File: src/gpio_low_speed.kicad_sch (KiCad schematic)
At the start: 3 parts, among them J1 RJ45_Amphenol_RJMG1BD3B8K1ANR, J2 Micro_SD_Card_Det2

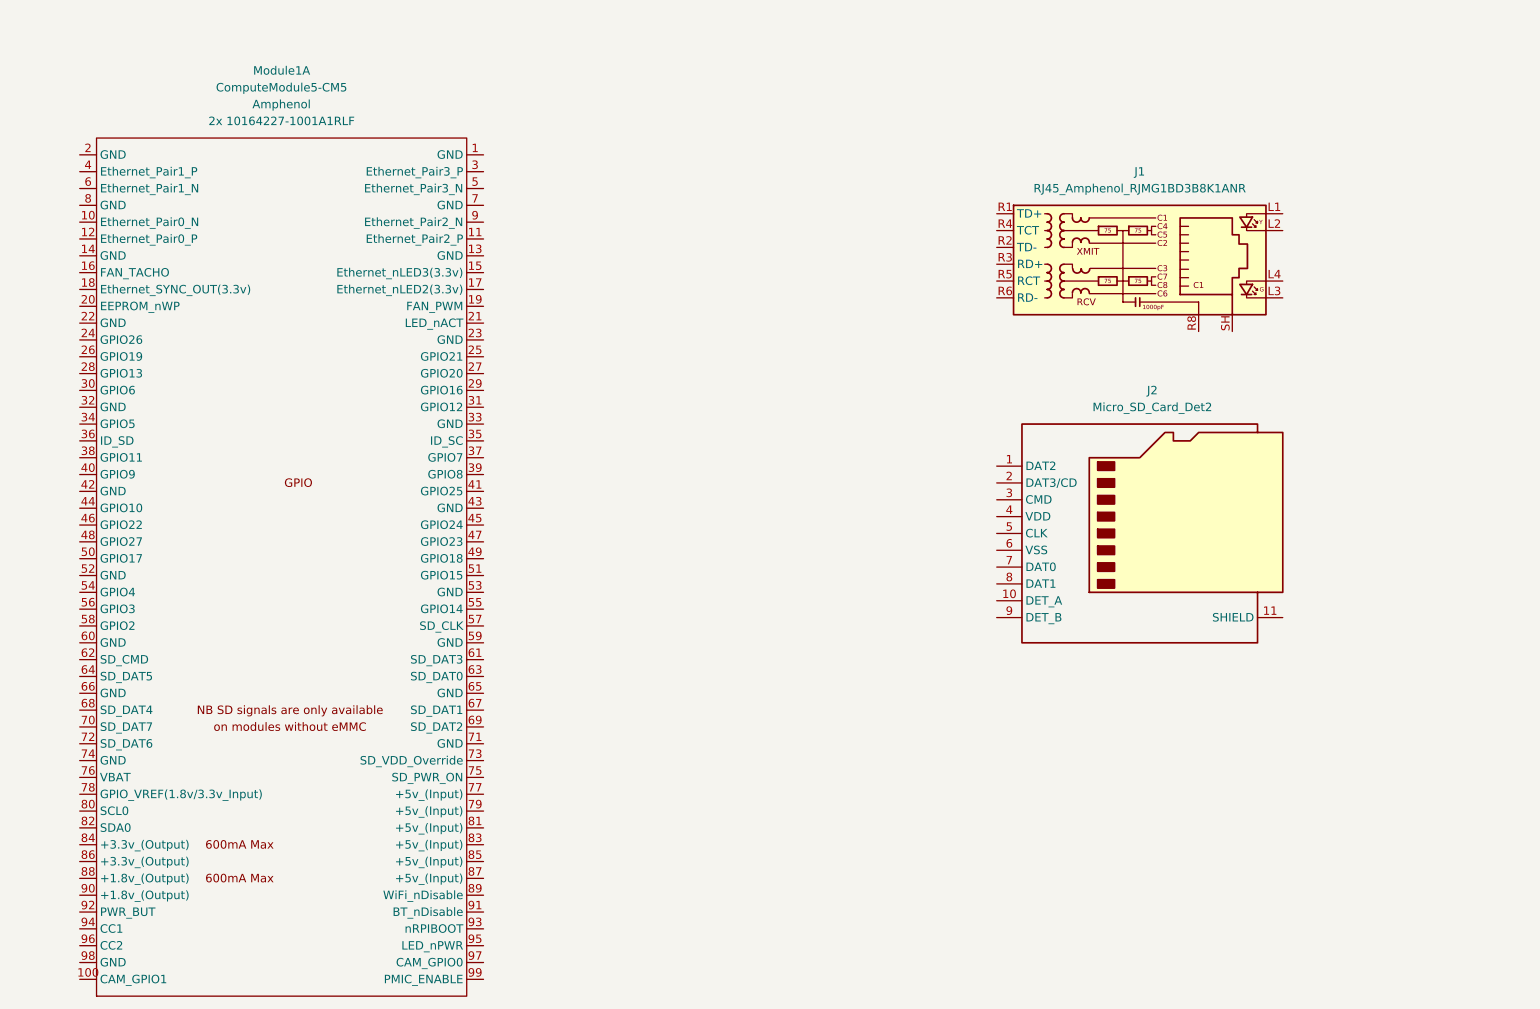
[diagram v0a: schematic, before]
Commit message: Add ethernet circuitry
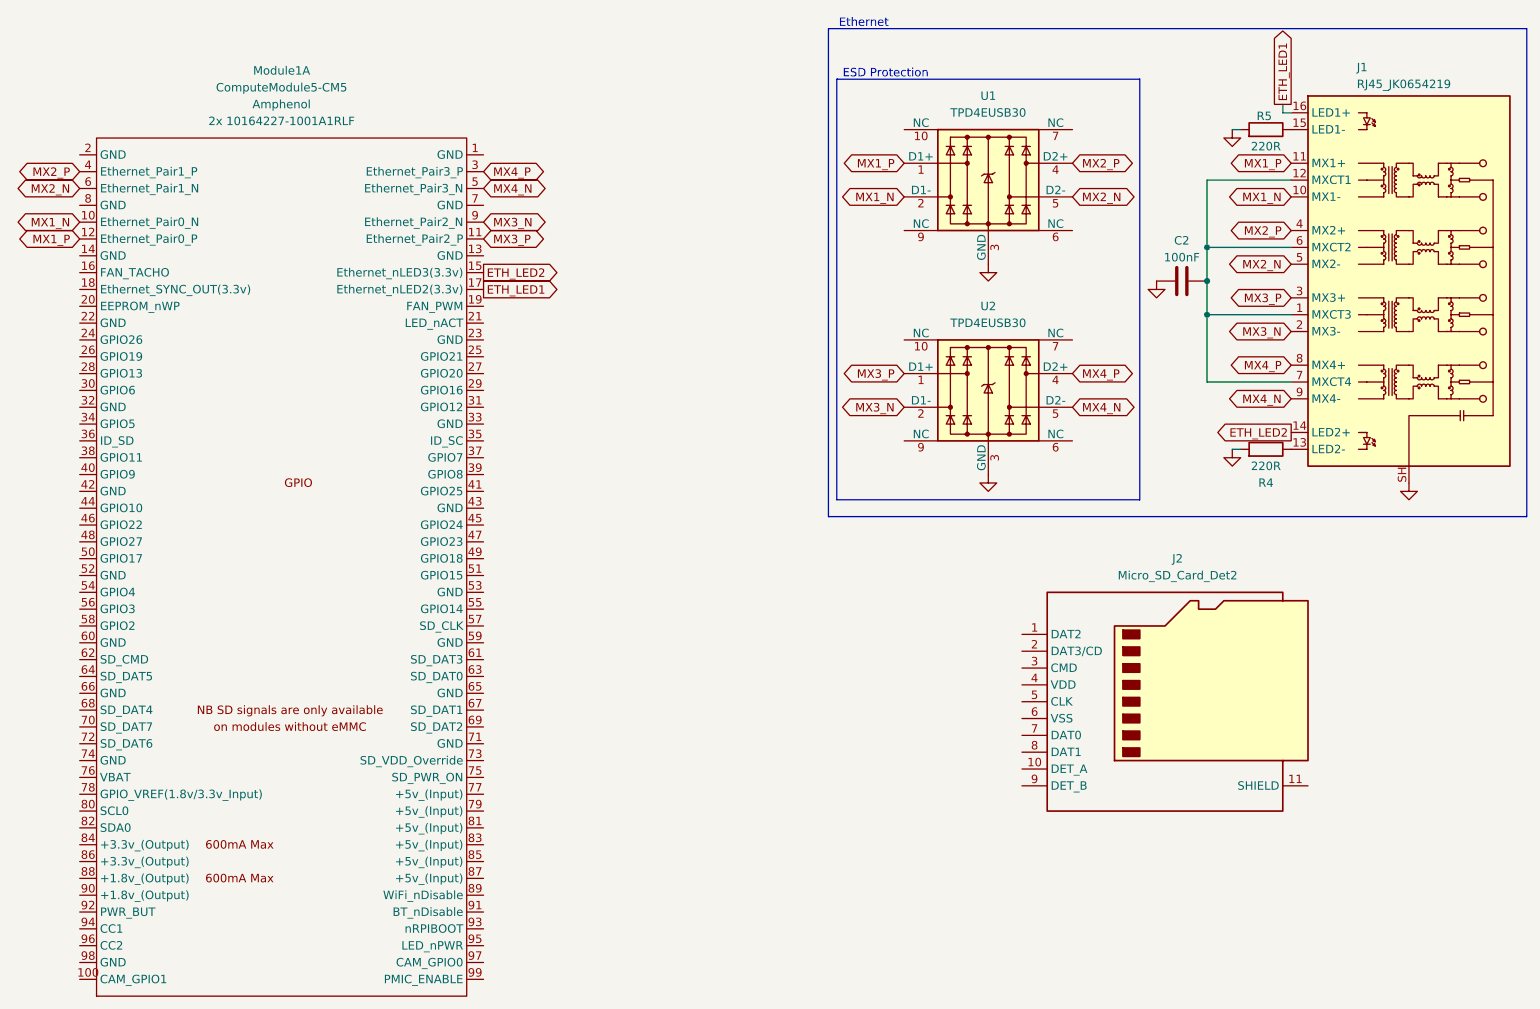
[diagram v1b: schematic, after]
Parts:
- removed J1: RJ45_Amphenol_RJMG1BD3B8K1ANR, Connector_RJ:RJ45_Amphenol_RJMG1BD3B8K1ANR, symbol Connector:RJ45_Amphenol_RJMG1BD3B8K1ANR
- added C2: 100nF, symbol Device:C
- added J1: RJ45_JK0654219, Connector_RJ:RJ45_Pulse_JK0654219NL_Horizontal, symbol Connector:RJ45_JK0654219
- added R4, R5: 220R, symbol Device:R
- added U1, U2: TPD4EUSB30, Package_SON:USON-10_2.5x1.0mm_P0.5mm, symbol Power_Protection:TPD4EUSB30
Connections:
- net MX1_N: now reaches Module1.10 (Ethernet_Pair0_N)
- net MX1_N: now also J1.10 (MX1-), U1.2 (D1-)
- net MX3_P: now reaches Module1.11 (Ethernet_Pair2_P)
- net MX3_P: now also J1.3 (MX3+), U2.1 (D1+)
- net MX1_P: now reaches Module1.12 (Ethernet_Pair0_P)
- net MX1_P: now also J1.11 (MX1+), U1.1 (D1+)
- net ETH_LED2: now reaches Module1.15 (Ethernet_nLED3(3.3v))
- net ETH_LED2: now also J1.14 (LED2+)
- net ETH_LED1: now reaches Module1.17 (Ethernet_nLED2(3.3v))
- net ETH_LED1: now also J1.16 (LED1+)
- net MX4_P: now reaches Module1.3 (Ethernet_Pair3_P)
- net MX4_P: now also J1.8 (MX4+), U2.4 (D2+)
- net MX2_P: now reaches Module1.4 (Ethernet_Pair1_P)
- net MX2_P: now also J1.4 (MX2+), U1.4 (D2+)
- net MX4_N: now reaches Module1.5 (Ethernet_Pair3_N)
- net MX4_N: now also J1.9 (MX4-), U2.5 (D2-)
- net MX2_N: now reaches Module1.6 (Ethernet_Pair1_N)
- net MX2_N: now also J1.5 (MX2-), U1.5 (D2-)
- net MX3_N: now reaches Module1.9 (Ethernet_Pair2_N)
- net MX3_N: now also J1.2 (MX3-), U2.2 (D1-)
- new net: C2.2, J1.1 (MXCT3), J1.12 (MXCT1), J1.6 (MXCT2), J1.7 (MXCT4)
- new net: J1.13 (LED2-), R4.1
- new net: J1.15 (LED1-), R5.1
- new net GND: C2.1, J1.SH, R4.2, R5.2, U1.3 (GND), U1.8 (GND), U2.3 (GND), U2.8 (GND)
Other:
- note added: "ESD Protection"
- note added: "Ethernet"
- moved on the sheet: J2

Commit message: Begin working on power solution for HDMI + SD
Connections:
- net SD_PWR_ON: now reaches Module1.75 (SD_PWR_ON)
- net SD_PWR: now reaches J2.1 (DAT2)
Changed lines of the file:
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@@
+		)
+	)
+	(hierarchical_label "SD_PWR"
+		(shape input)
+		(at 205.74 106.68 180)
+		(fields_autoplaced yes)
+		(effects
+			(font
+				(size 1.27 1.27)
+			)
+			(justify right)
+		)
+	)
+	(hierarchical_label "SD_PWR_ON"
+		(shape output)
+		(at 124.46 128.27 0)
+		(fields_autoplaced yes)
+		(effects
+			(font
+				(size 1.27 1.27)
+			)
+			(justify left)
 		)
 	)
